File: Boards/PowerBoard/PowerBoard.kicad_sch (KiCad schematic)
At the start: 0 parts

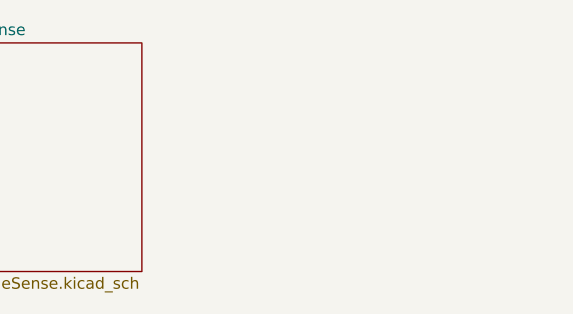
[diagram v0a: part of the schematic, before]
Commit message: Add Zeners to Power Board
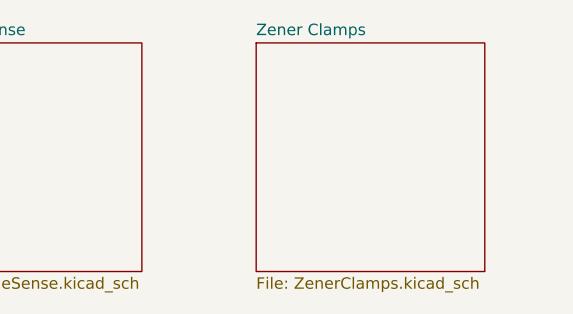
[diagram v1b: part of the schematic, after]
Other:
- added sheet Zener Clamps (ZenerClamps.kicad_sch)
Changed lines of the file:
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@@
+	)
+	(sheet
+		(at 177.8 25.4)
+		(size 25.4 25.4)
+		(exclude_from_sim no)
+		(in_bom yes)
+		(on_board yes)
+		(dnp no)
+		(fields_autoplaced yes)
+		(stroke
+			(width 0.1524)
+			(type solid)
+		)
+		(fill
+			(color 0 0 0 0.0000)
+		)
+		(property "Sheetname" "Zener Clamps"
+			(at 177.8 24.6884 0)
+			(effects
+				(font
+					(size 1.27 1.27)
+				)
+				(justify left bottom)
+			)
+		)
+		(property "Sheetfile" "ZenerClamps.kicad_sch"
+			(at 177.8 51.3846 0)
+			(effects
+				(font
+					(size 1.27 1.27)
+				)
+				(justify left top)
+			)
+		)
+		(property "Field2" ""
+			(at 177.8 25.4 0)
+			(effects
+				(font
+					(size 1.27 1.27)
+				)
+			)
+		)
+		(instances
+			(project "PowerBoard"
+				(path "/80d633a3-2bf5-410b-b8ea-b291012109f7"
+					(page "6")
+				)
+			)
+		)
 	)
 	(sheet
